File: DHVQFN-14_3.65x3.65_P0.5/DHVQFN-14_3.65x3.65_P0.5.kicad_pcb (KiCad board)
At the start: 2 copper layers, 20.3 x 22.9 mm, 6 parts, among them J101 Conn_01x09, J102 Conn_01x09, J103 Conn_01x12, J104 Conn_01x09, U101 DHVQFN-14

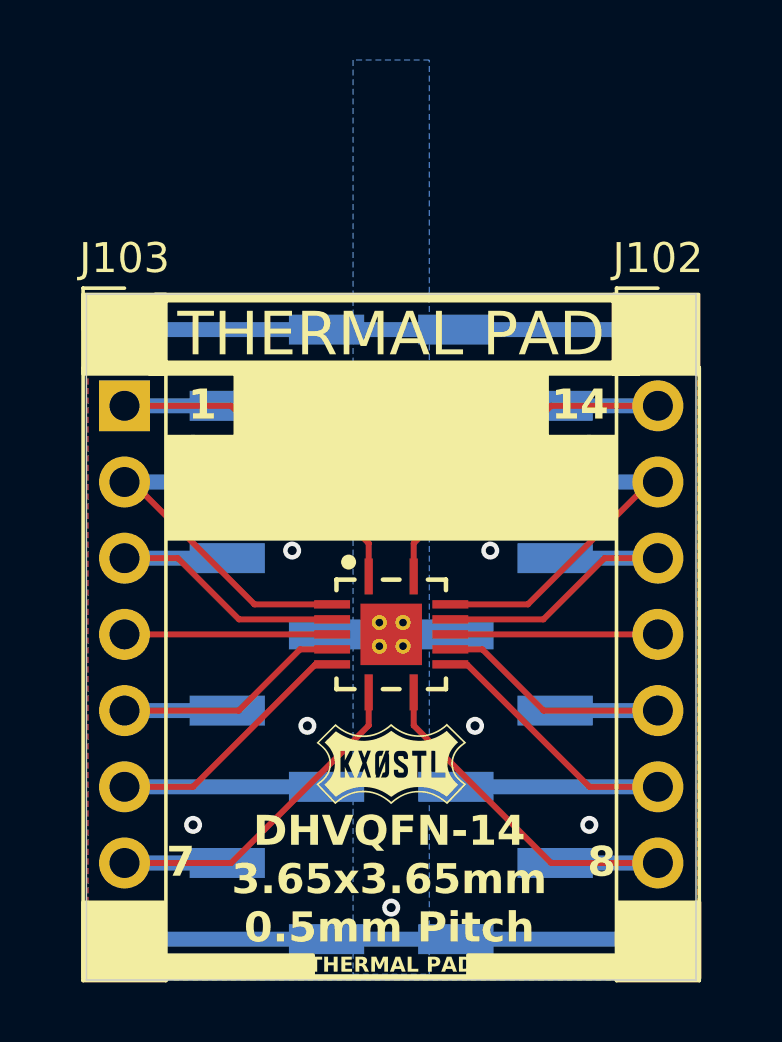
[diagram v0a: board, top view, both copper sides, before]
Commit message: Created SMDIP-16, QFP-48, QFP-32, QFN-80, QFN-68, QFN-64, QFN-60, QFN-56, QFN-48, QFN-36, QFN-28, QFN-20, QFP-32, QFP-48
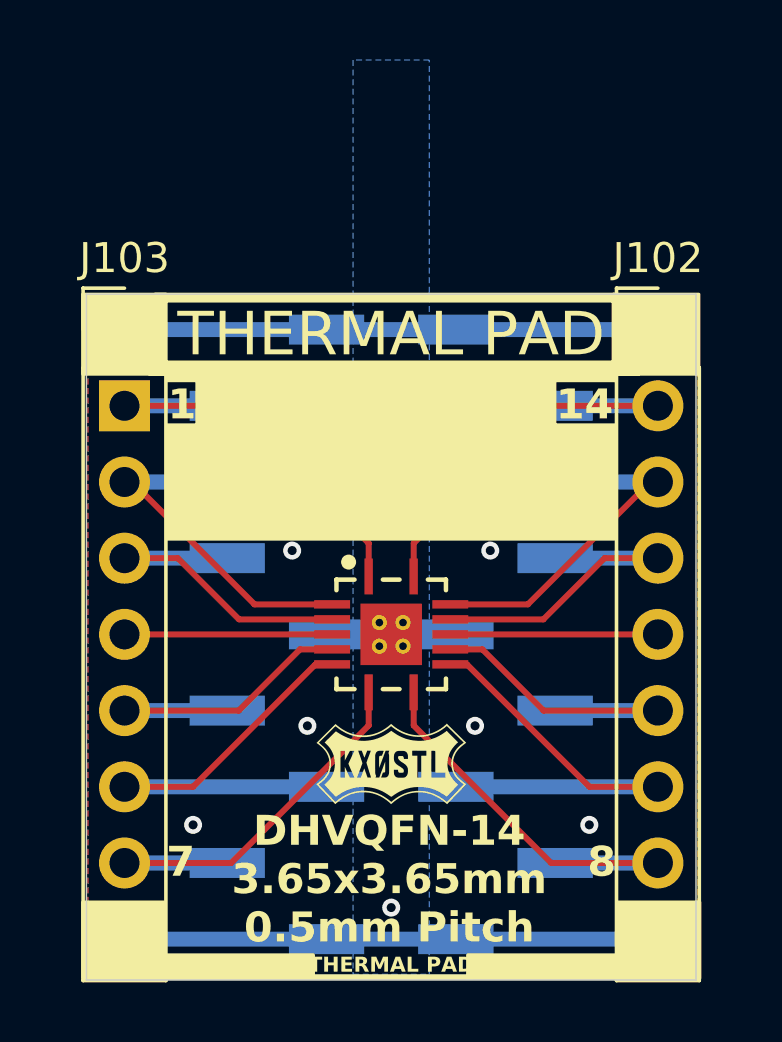
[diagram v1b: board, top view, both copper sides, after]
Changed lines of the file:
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@@
 	)
 	(gr_rect
-		(start 125.603 104.648)
+		(start 125.603 104.268)
 		(end 140.589 108.077)
 		(stroke
@@
 	)
 	(gr_rect
-		(start 127.889 102.489)
-		(end 138.303 106.68)
+		(start 126.619 102.489)
+		(end 138.553 106.68)
+		(stroke
+			(width 0.1)
+			(type solid)
+		)
+		(fill yes)
+		(layer "F.SilkS")
+	)
+	(gr_rect
+		(start 125.623 102.5045)
+		(end 140.577 102.7955)
 		(stroke
 			(width 0.1)
@@
 	)
 	(gr_text "14"
-		(at 139.389 103.595274 0)
-		(layer "F.SilkS")
+		(at 139.54 103.59 0)
+		(layer "F.SilkS" knockout)
 		(effects
 			(font
@@
 	)
 	(gr_text "1"
-		(at 126.803 103.595274 0)
-		(layer "F.SilkS")
+		(at 126.12 103.59 0)
+		(layer "F.SilkS" knockout)
 		(effects
 			(font
